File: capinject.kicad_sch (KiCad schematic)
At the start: 0 parts

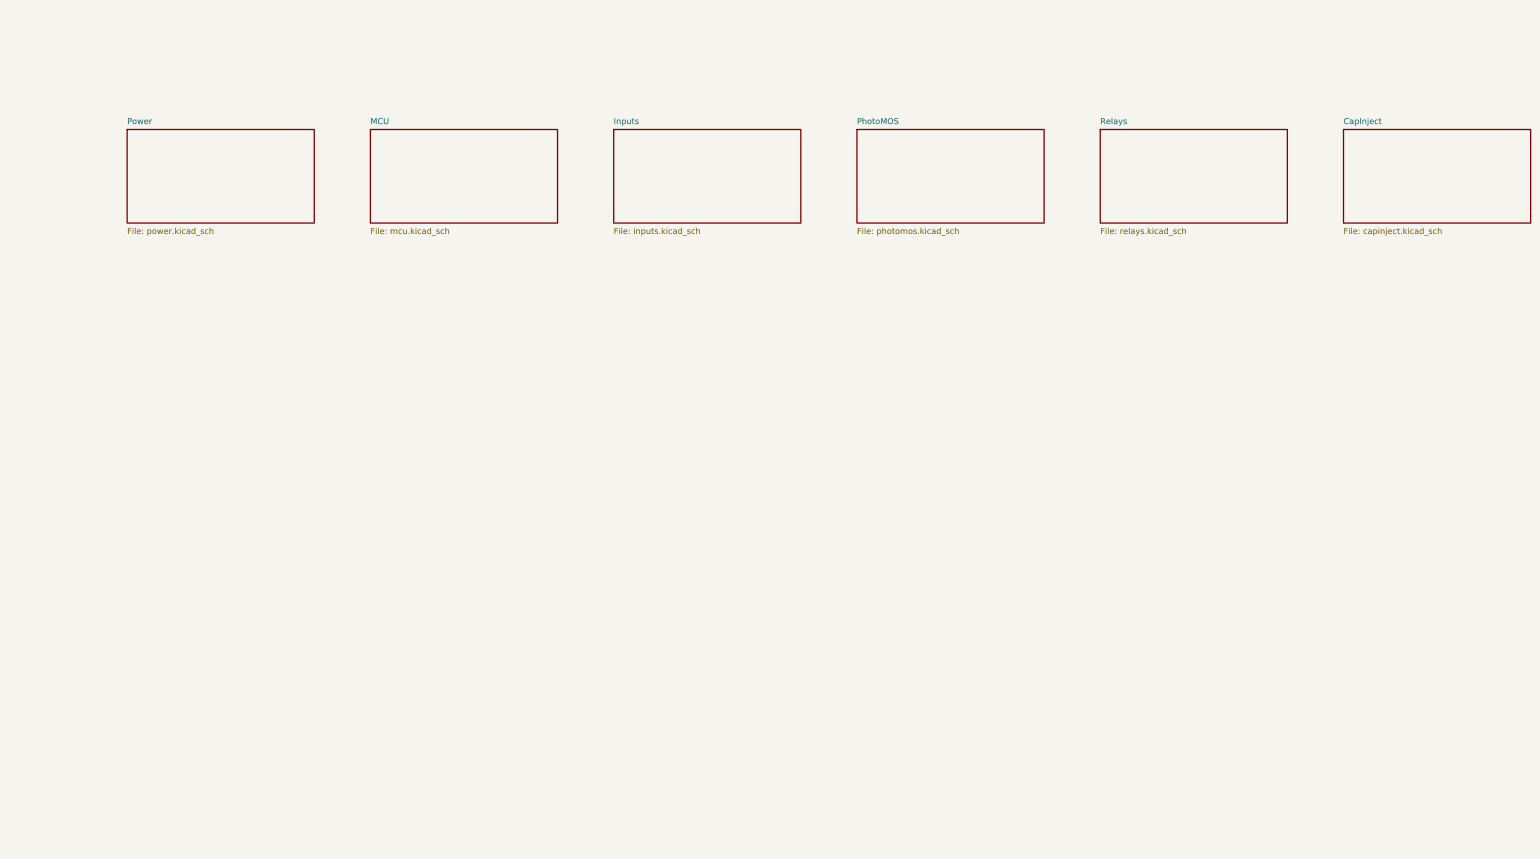
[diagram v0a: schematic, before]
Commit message: Realize ERC-clean KiCad schematic (rev 0.2)
Turn the paper design into a real KiCad 10 hierarchical schematic with
library symbols and footprints. 6 sheets: power, MCU, and full channel
counts (8 inputs, 8 PhotoMOS, 2 relays, 4 cap-inject) = 160 components.

- Replace AMS1117 with SY8089 buck (2.7-5.5Vin) for Wi-Fi-peak headroom.
- Input front-end uses 2.2k/1206 + EL357N (CRD dropped; poor LCSC stock).
- Verify key parts against JLCPCB (ESP32-S3 C2913198, SY8089 C78988,
  AQY212GS C719745, HK4100F C12072, USB-C C165948, AO3400A C20917).
- ERC passes 0 errors / 0 warnings; netlist verified, isolation barrier
  confirmed intact. No PCB layout yet (per request).
- Add Python generator (gen/) that emits the project and custom symbols.

Co-Authored-By: Claude Opus 4.7 <noreply@anthropic.com>
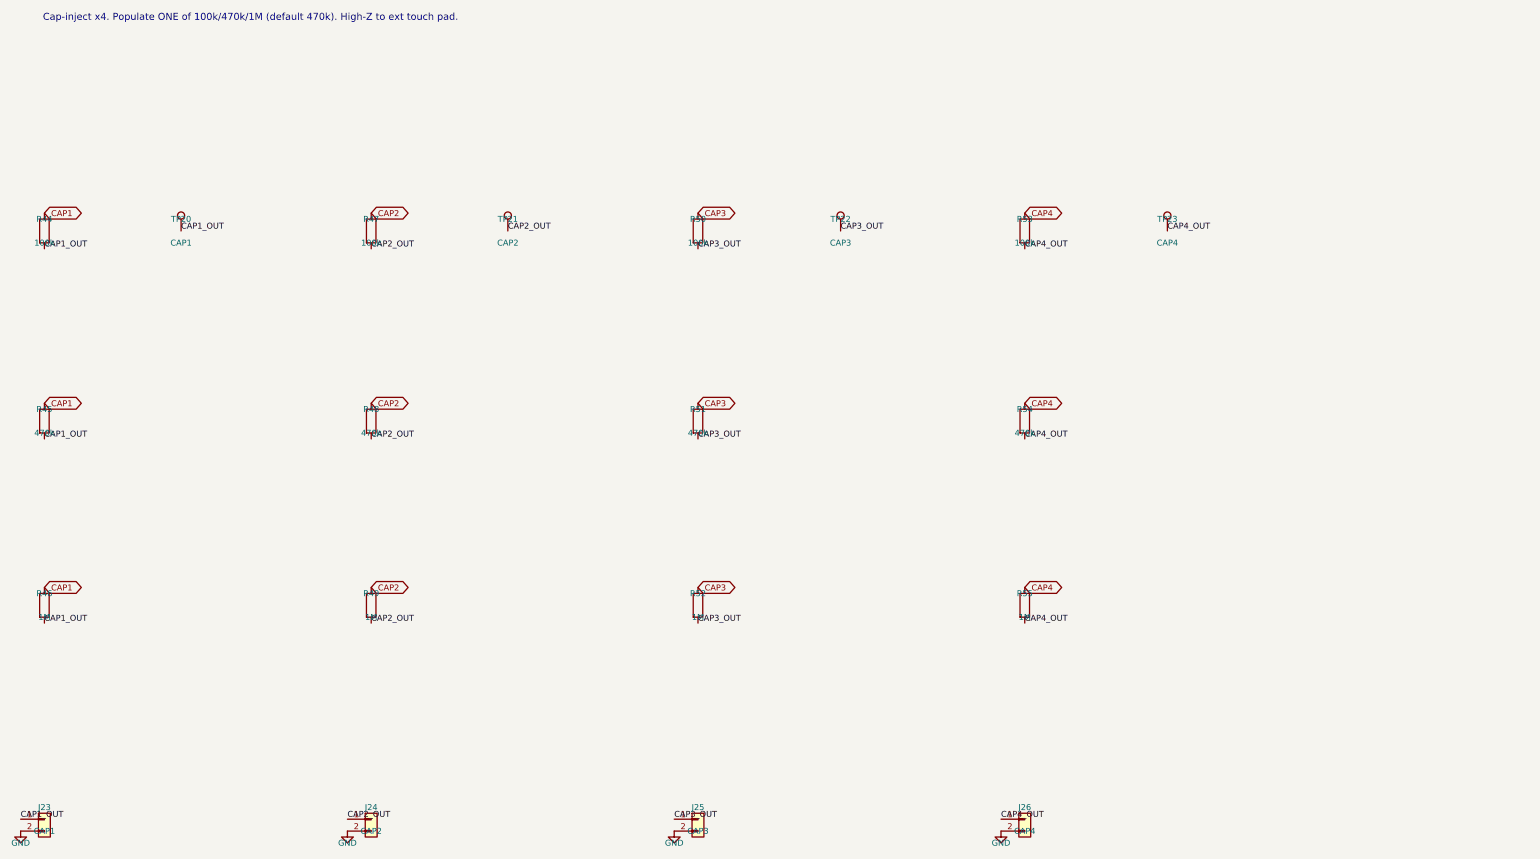
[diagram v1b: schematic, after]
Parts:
- added J23: CAP1, TerminalBlock:TerminalBlock_MaiXu_MX126-5.0-02P_1x02_P5.00mm, symbol Connector_Generic:Conn_01x02
- added J24: CAP2, TerminalBlock:TerminalBlock_MaiXu_MX126-5.0-02P_1x02_P5.00mm, symbol Connector_Generic:Conn_01x02
- added J25: CAP3, TerminalBlock:TerminalBlock_MaiXu_MX126-5.0-02P_1x02_P5.00mm, symbol Connector_Generic:Conn_01x02
- added J26: CAP4, TerminalBlock:TerminalBlock_MaiXu_MX126-5.0-02P_1x02_P5.00mm, symbol Connector_Generic:Conn_01x02
- added R44, R47, R50, R53: 100k, Resistor_SMD:R_0603_1608Metric, symbol Device:R
- added R45, R48, R51, R54: 470k, Resistor_SMD:R_0603_1608Metric, symbol Device:R
- added R46, R49, R52, R55: 1M, Resistor_SMD:R_0603_1608Metric, symbol Device:R
- added TP20: CAP1, TestPoint:TestPoint_Pad_D1.5mm, symbol Connector:TestPoint
- added TP21: CAP2, TestPoint:TestPoint_Pad_D1.5mm, symbol Connector:TestPoint
- added TP22: CAP3, TestPoint:TestPoint_Pad_D1.5mm, symbol Connector:TestPoint
- added TP23: CAP4, TestPoint:TestPoint_Pad_D1.5mm, symbol Connector:TestPoint
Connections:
- new net CAP1: R44.1, R45.1, R46.1
- new net CAP1_OUT: J23.1 (Pin_1), R44.2, R45.2, R46.2, TP20.1
- new net CAP2: R47.1, R48.1, R49.1
- new net CAP2_OUT: J24.1 (Pin_1), R47.2, R48.2, R49.2, TP21.1
- new net CAP3: R50.1, R51.1, R52.1
- new net CAP3_OUT: J25.1 (Pin_1), R50.2, R51.2, R52.2, TP22.1
- new net CAP4: R53.1, R54.1, R55.1
- new net CAP4_OUT: J26.1 (Pin_1), R53.2, R54.2, R55.2, TP23.1
- new net GND: J23.2 (Pin_2), J24.2 (Pin_2), J25.2 (Pin_2), J26.2 (Pin_2)
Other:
- removed sheet CapInject
- removed sheet Inputs
- removed sheet MCU
- removed sheet PhotoMOS
- removed sheet Power
- removed sheet Relays
- note added: "Cap-inject x4. Populate ONE of 100k/470k/1M (default 470k). High-Z to ext touch pad."
- title: Universal ESP32 Button/Signal Bridge -> 4x capacitive injection outputs

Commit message: Add real footprints (HK4100F/AQY212GS/EL357N) + tidy schematic (rev 0.3)
- Build datasheet-accurate HK4100F-DC5V-SHG footprint (6-pad THT) and a
  matching symbol; coil=3/4, COM=5/6, NO=1, NC=2.
- Correct AQY212GS footprint to SOP-4 2.54mm pitch (was wrongly 1.27mm).
- Fix EL357N LCSC code C124981->C6649 (C124981 was a trimmer pot); add
  generated SOP-4 footprint.
- footprints/bridge.pretty generated from LCSC parts via easyeda2kicad.
- Re-lay-out all sheets for human review: labels offset from pins via
  short stubs routed by each pin's true orientation; 8-channel sheets on
  larger pages; clean per-channel columns.
- ERC still 0 errors / 0 warnings. Regenerated schematic.pdf, BOM, DESIGN.
- No PCB layout yet (paused per request).

Co-Authored-By: Claude Opus 4.7 <noreply@anthropic.com>
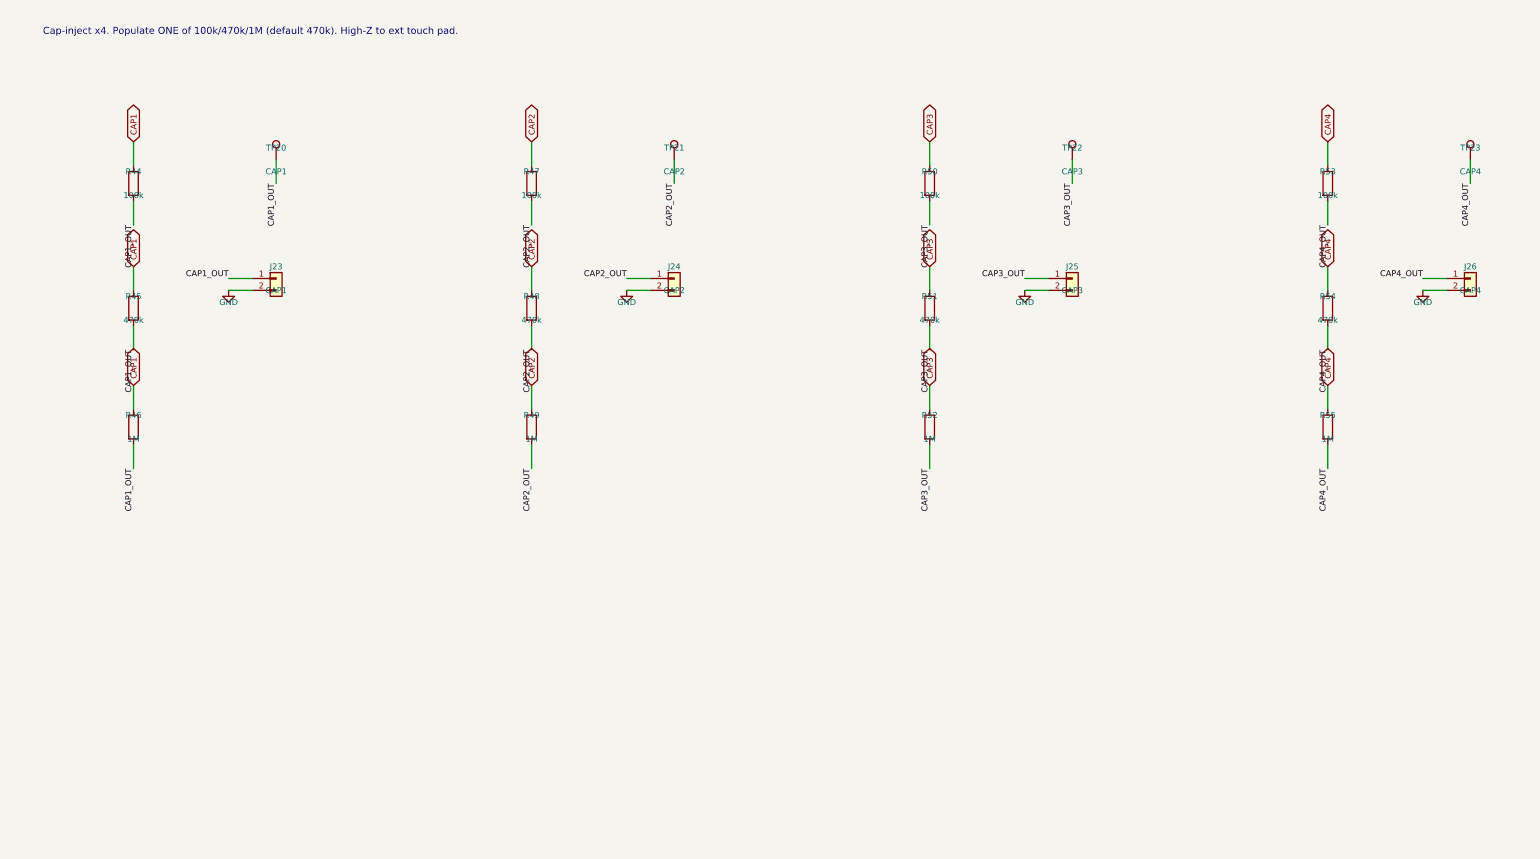
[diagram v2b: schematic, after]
